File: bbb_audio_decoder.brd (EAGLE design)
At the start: 110.5 x 100 mm, 183 parts, among them IC1 OPA2134, IC2 LM317, IC3 LM337, IC4 OPA2134, IC5 OPA2134, IC6 OPA2134, P1 PLR135/T9, P9 P9, Q1 BS170, Q2 BS170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

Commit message: Made gebers of ver1
(and snuck in a component value change, because it was a bug and is still
part of ver1)
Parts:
- R10, R11: value 68 -> 120
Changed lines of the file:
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@@
 <attribute name="NAME" x="107.47375" y="83.34375" size="1.27" layer="25" ratio="10"/>
 </element>
-<element name="R10" library="rcl" package="0204V" value="68" x="102.07625" y="88.10625" smashed="yes">
+<element name="R10" library="rcl" package="0204V" value="120" x="102.07625" y="88.10625" smashed="yes">
 <attribute name="NAME" x="100.4189" y="89.27465" size="1.27" layer="25" ratio="10"/>
 <attribute name="VALUE" x="99.94265" y="85.79485" size="1.27" layer="27" ratio="10"/>
@@
 <attribute name="NAME" x="95.5675" y="83.185" size="1.27" layer="25" ratio="10"/>
 </element>
-<element name="R11" library="rcl" package="0204V" value="68" x="92.075" y="88.10625" smashed="yes">
+<element name="R11" library="rcl" package="0204V" value="120" x="92.075" y="88.10625" smashed="yes">
 <attribute name="NAME" x="90.10015" y="85.6234" size="1.27" layer="25" ratio="10"/>
 <attribute name="VALUE" x="89.9414" y="85.79485" size="1.27" layer="27" ratio="10"/>

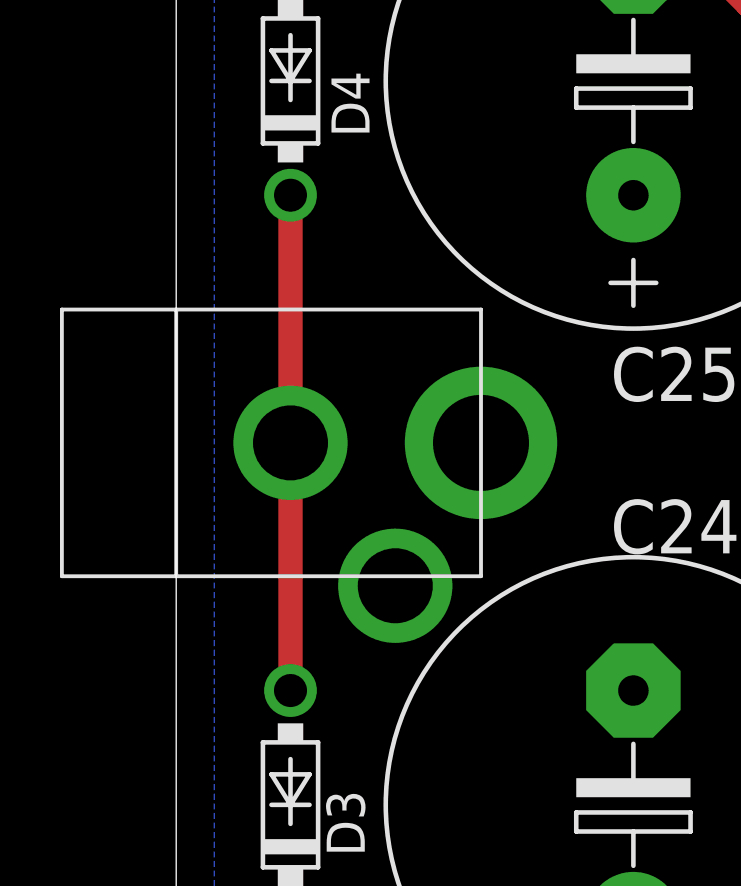
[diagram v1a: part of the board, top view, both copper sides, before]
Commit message: Renamed 5.5 mm adapter symbol
This one specifies the inner diameter too.
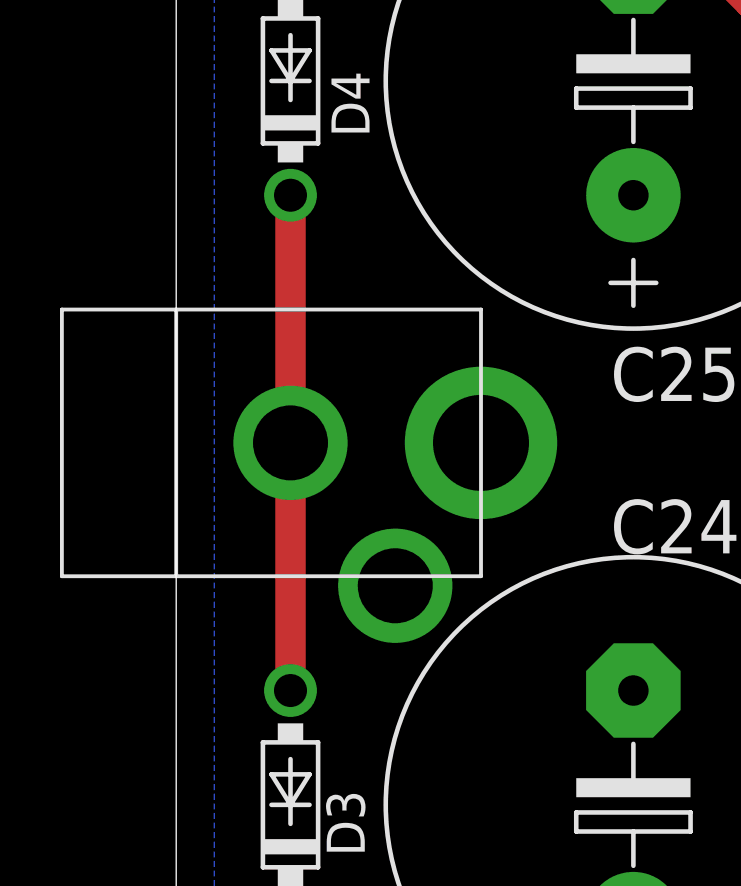
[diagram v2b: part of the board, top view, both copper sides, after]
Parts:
- AC: value ADAPTER-PLUG-5.5MM -> ADAPTER-PLUG-5.5/2.1MM; device 0000halfgaar:ADAPTER-PLUG-5.5MM -> 0000halfgaar:ADAPTER-PLUG-5.5/2.1MM
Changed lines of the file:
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@@
 <attribute name="VALUE" x="88.011" y="8.763" size="1.27" layer="27" ratio="10"/>
 </element>
-<element name="AC" library="0000halfgaar" package="ADAPTER-PLUG-5.5MM" value="ADAPTER-PLUG-5.5MM" x="-3.81" y="72.39" rot="R90"/>
 <element name="C33" library="rcl" package="E2,5-6" value="22µF/25V" x="28.8925" y="96.52" smashed="yes" rot="R270">
 <attribute name="NAME" x="22.987" y="97.7265" size="1.27" layer="25" ratio="10"/>
@@
 <attribute name="VALUE" x="54.61" y="84.201" size="1.27" layer="27" ratio="10"/>
 </element>
+<element name="AC" library="0000halfgaar" package="ADAPTER-PLUG-5.5/2.1MM" value="ADAPTER-PLUG-5.5/2.1MM" x="-3.81" y="72.39" rot="R90"/>
 </elements>
 <signals>
@@
 <contactref element="R24" pad="1"/>
 <contactref element="C27" pad="1"/>
-<contactref element="AC" pad="3"/>
 <contactref element="3_C5" pad="1"/>
 <contactref element="3_R5" pad="1"/>
@@
 <contactref element="OUT8" pad="1"/>
 <contactref element="OUT7" pad="1"/>
+<contactref element="AC" pad="3"/>
 </signal>
 <signal name="VCC">
@@
 <contactref element="D4" pad="C"/>
 <contactref element="AC" pad="1"/>
-<wire x1="3.81" y1="68.58" x2="3.81" y2="76.835" width="0.8128" layer="1"/>
-<wire x1="3.81" y1="76.835" x2="3.81" y2="85.09" width="0.8128" layer="1"/>
+<wire x1="3.81" y1="68.58" x2="3.81" y2="76.835" width="1.016" layer="1"/>
+<wire x1="3.81" y1="76.835" x2="3.81" y2="85.09" width="1.016" layer="1"/>
 </signal>
 <signal name="N$41">

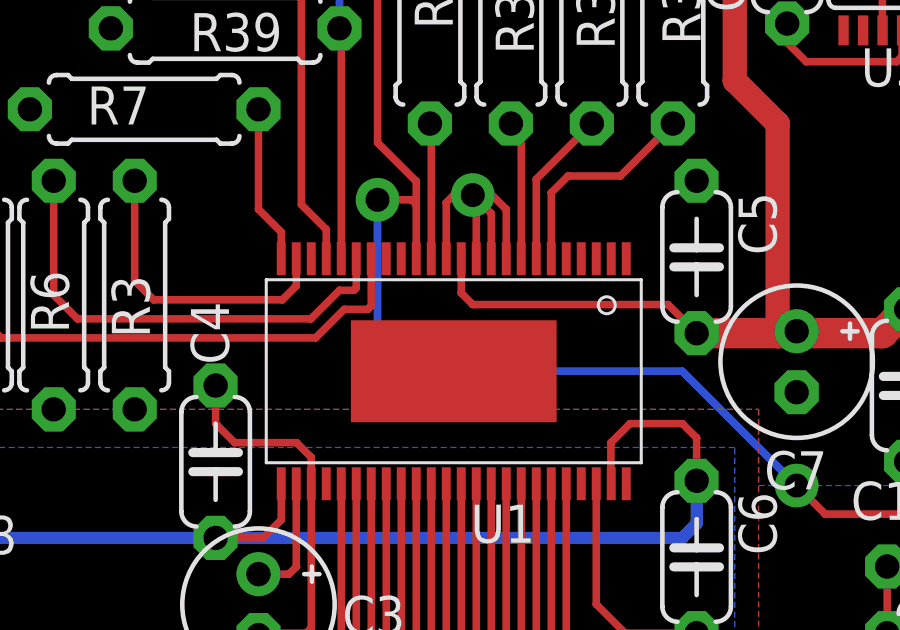
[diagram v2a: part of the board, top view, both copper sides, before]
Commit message: Use updated PCM1690 package
Description was wrong, and the thermal pad wasn't connected.
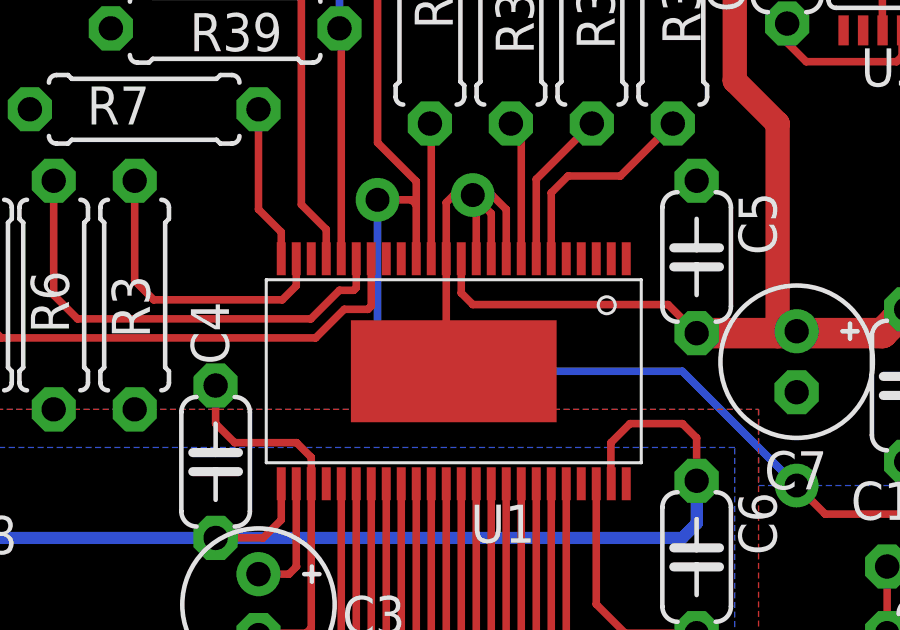
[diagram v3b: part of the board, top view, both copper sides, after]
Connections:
- net DGND: now also U1.EXP
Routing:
- net DGND: track 48.4 -> 52.3 mm
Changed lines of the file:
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@@
 <contactref element="C16" pad="-"/>
 <via x="62.865" y="73.18375" extent="1-16" drill="0.8"/>
-<wire x1="61.98" y1="71.06" x2="61.98" y2="72.93375" width="0.254" layer="1"/>
 <wire x1="61.98" y1="72.93375" x2="62.23" y2="73.18375" width="0.254" layer="1"/>
 <wire x1="62.23" y1="73.18375" x2="62.865" y2="73.18375" width="0.254" layer="1"/>
@@
 <contactref element="Q2" pad="S"/>
 <contactref element="C17" pad="-"/>
+<contactref element="U1" pad="EXP"/>
+<wire x1="61.98" y1="71.06" x2="61.98" y2="67.56" width="0.254" layer="1"/>
+<wire x1="61.98" y1="67.56" x2="62.23" y2="67.31" width="0.254" layer="1"/>
+<wire x1="61.98" y1="71.06" x2="61.98" y2="72.93375" width="0.254" layer="1"/>
 </signal>
 <signal name="AGND">

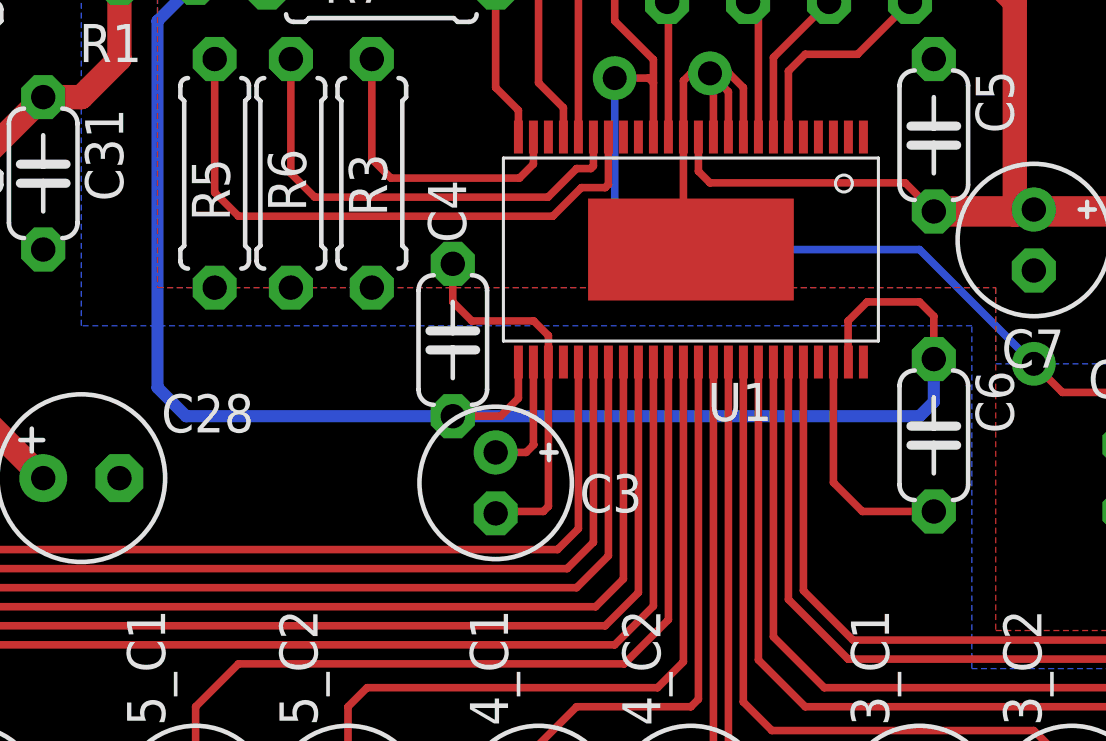
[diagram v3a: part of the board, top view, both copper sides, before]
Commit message: Moved C3 and C4 a bit apart
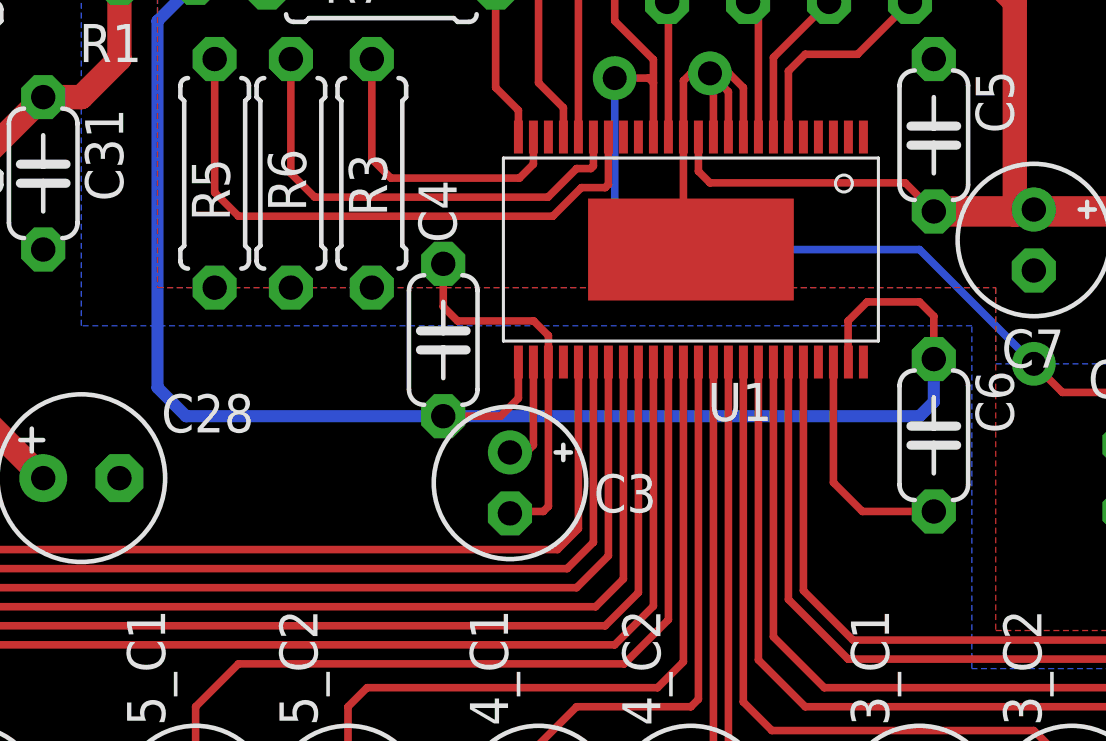
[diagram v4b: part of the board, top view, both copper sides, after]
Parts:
- moved C3 0.48 mm to (56.2, 59.5)
- moved C4 0.32 mm to (54.0, 64.3)
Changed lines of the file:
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@@
 <attribute name="VALUE" x="66.205" y="68.58" size="1.27" layer="27" rot="R180"/>
 </element>
-<element name="C3" library="rcl" package="E2-5" value="10 µF" x="55.72125" y="59.53125" smashed="yes" rot="R270">
-<attribute name="NAME" x="58.51525" y="58.547" size="1.27" layer="25" ratio="10"/>
-<attribute name="VALUE" x="53.94325" y="57.37225" size="1.27" layer="27" ratio="10" rot="R270"/>
-</element>
-<element name="C4" library="rcl" package="C050-024X044" value="1µF ml" x="54.2925" y="64.29375" smashed="yes" rot="R270">
-<attribute name="NAME" x="53.467" y="69.62775" size="1.27" layer="25" ratio="10" rot="R270"/>
-<attribute name="VALUE" x="51.6255" y="66.45275" size="1.27" layer="27" ratio="10" rot="R270"/>
+<element name="C3" library="rcl" package="E2-5" value="10 µF" x="56.1975" y="59.53125" smashed="yes" rot="R270">
+<attribute name="NAME" x="58.9915" y="58.547" size="1.27" layer="25" ratio="10"/>
+<attribute name="VALUE" x="54.4195" y="57.37225" size="1.27" layer="27" ratio="10" rot="R270"/>
+</element>
+<element name="C4" library="rcl" package="C050-024X044" value="1µF ml" x="53.975" y="64.29375" smashed="yes" rot="R270">
+<attribute name="NAME" x="53.1495" y="69.62775" size="1.27" layer="25" ratio="10" rot="R270"/>
+<attribute name="VALUE" x="51.308" y="66.45275" size="1.27" layer="27" ratio="10" rot="R270"/>
 </element>
 <element name="C5" library="rcl" package="C050-024X044" value="1µF ml" x="70.32625" y="71.12" rot="R270"/>
@@
 <wire x1="57.48" y1="63.56" x2="57.48" y2="64.44" width="0.254" layer="1"/>
 <wire x1="57.48" y1="64.44" x2="56.99125" y2="64.92875" width="0.254" layer="1"/>
-<wire x1="56.99125" y1="64.92875" x2="54.9275" y2="64.92875" width="0.254" layer="1"/>
-<wire x1="54.9275" y1="64.92875" x2="54.2925" y2="65.56375" width="0.254" layer="1"/>
-<wire x1="54.2925" y1="65.56375" x2="54.2925" y2="66.83375" width="0.254" layer="1"/>
+<wire x1="56.99125" y1="64.92875" x2="54.45125" y2="64.92875" width="0.254" layer="1"/>
 <contactref element="JP3" pad="2"/>
 <wire x1="57.48" y1="63.56" x2="57.48" y2="58.75" width="0.254" layer="1"/>
 <wire x1="57.48" y1="58.75" x2="57.30875" y2="58.57875" width="0.254" layer="1"/>
-<wire x1="57.30875" y1="58.57875" x2="55.78475" y2="58.57875" width="0.254" layer="1"/>
-<wire x1="55.78475" y1="58.57875" x2="55.72125" y2="58.51525" width="0.254" layer="1"/>
 <contactref element="OUT1" pad="1"/>
 <contactref element="OUT4" pad="1"/>
@@
 <contactref element="OUT7" pad="1"/>
 <contactref element="AC" pad="3"/>
+<wire x1="54.45125" y1="64.92875" x2="53.975" y2="65.405" width="0.254" layer="1"/>
+<wire x1="53.975" y1="65.405" x2="53.975" y2="66.83375" width="0.254" layer="1"/>
+<wire x1="57.30875" y1="58.57875" x2="56.261" y2="58.57875" width="0.254" layer="1"/>
+<wire x1="56.261" y1="58.57875" x2="56.1975" y2="58.51525" width="0.254" layer="1"/>
 </signal>
 <signal name="VCC">
@@
 <wire x1="44.45" y1="74.93" x2="44.45" y2="62.70625" width="0.4064" layer="16"/>
 <wire x1="44.45" y1="62.70625" x2="45.4025" y2="61.75375" width="0.4064" layer="16"/>
-<wire x1="45.4025" y1="61.75375" x2="54.2925" y2="61.75375" width="0.4064" layer="16"/>
+<wire x1="45.4025" y1="61.75375" x2="53.975" y2="61.75375" width="0.4064" layer="16"/>
 <wire x1="69.85" y1="65.56375" x2="68.10375" y2="65.56375" width="0.254" layer="1"/>
 <wire x1="68.10375" y1="65.56375" x2="67.46875" y2="64.92875" width="0.254" layer="1"/>
 <wire x1="67.46875" y1="64.92875" x2="67.46875" y2="63.57125" width="0.254" layer="1"/>
 <wire x1="67.46875" y1="63.57125" x2="67.48" y2="63.56" width="0.254" layer="1"/>
-<wire x1="54.2925" y1="61.75375" x2="69.85" y2="61.75375" width="0.4064" layer="16"/>
+<wire x1="53.975" y1="61.75375" x2="69.85" y2="61.75375" width="0.4064" layer="16"/>
 <wire x1="69.85" y1="65.56375" x2="70.32625" y2="65.0875" width="0.254" layer="1"/>
 <wire x1="70.32625" y1="65.0875" x2="70.32625" y2="63.65875" width="0.254" layer="1"/>
 <wire x1="56.48" y1="63.56" x2="56.48" y2="62.35375" width="0.254" layer="1"/>
 <wire x1="56.48" y1="62.35375" x2="55.88" y2="61.75375" width="0.254" layer="1"/>
-<wire x1="55.88" y1="61.75375" x2="54.2925" y2="61.75375" width="0.254" layer="1"/>
+<wire x1="55.88" y1="61.75375" x2="53.975" y2="61.75375" width="0.254" layer="1"/>
 <wire x1="69.85" y1="61.75375" x2="70.32625" y2="62.23" width="0.4064" layer="16"/>
 <wire x1="70.32625" y1="62.23" x2="70.32625" y2="63.65875" width="0.4064" layer="16"/>
@@
 <contactref element="U1" pad="26"/>
 <contactref element="C3" pad="+"/>
-<wire x1="55.72125" y1="60.54725" x2="56.73725" y2="60.54725" width="0.254" layer="1"/>
-<wire x1="56.73725" y1="60.54725" x2="56.99125" y2="60.80125" width="0.254" layer="1"/>
-<wire x1="56.98" y1="63.56" x2="56.98" y2="60.8125" width="0.254" layer="1"/>
-<wire x1="56.98" y1="60.8125" x2="56.99125" y2="60.80125" width="0.254" layer="1"/>
+<wire x1="56.1975" y1="60.54725" x2="56.73725" y2="60.54725" width="0.254" layer="1"/>
+<wire x1="56.98" y1="63.56" x2="56.98" y2="60.79" width="0.254" layer="1"/>
+<wire x1="56.98" y1="60.79" x2="56.73725" y2="60.54725" width="0.254" layer="1"/>
 </signal>
 <signal name="N$11">
